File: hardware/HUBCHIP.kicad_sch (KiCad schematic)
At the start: 42 parts, among them Y1 25MHz

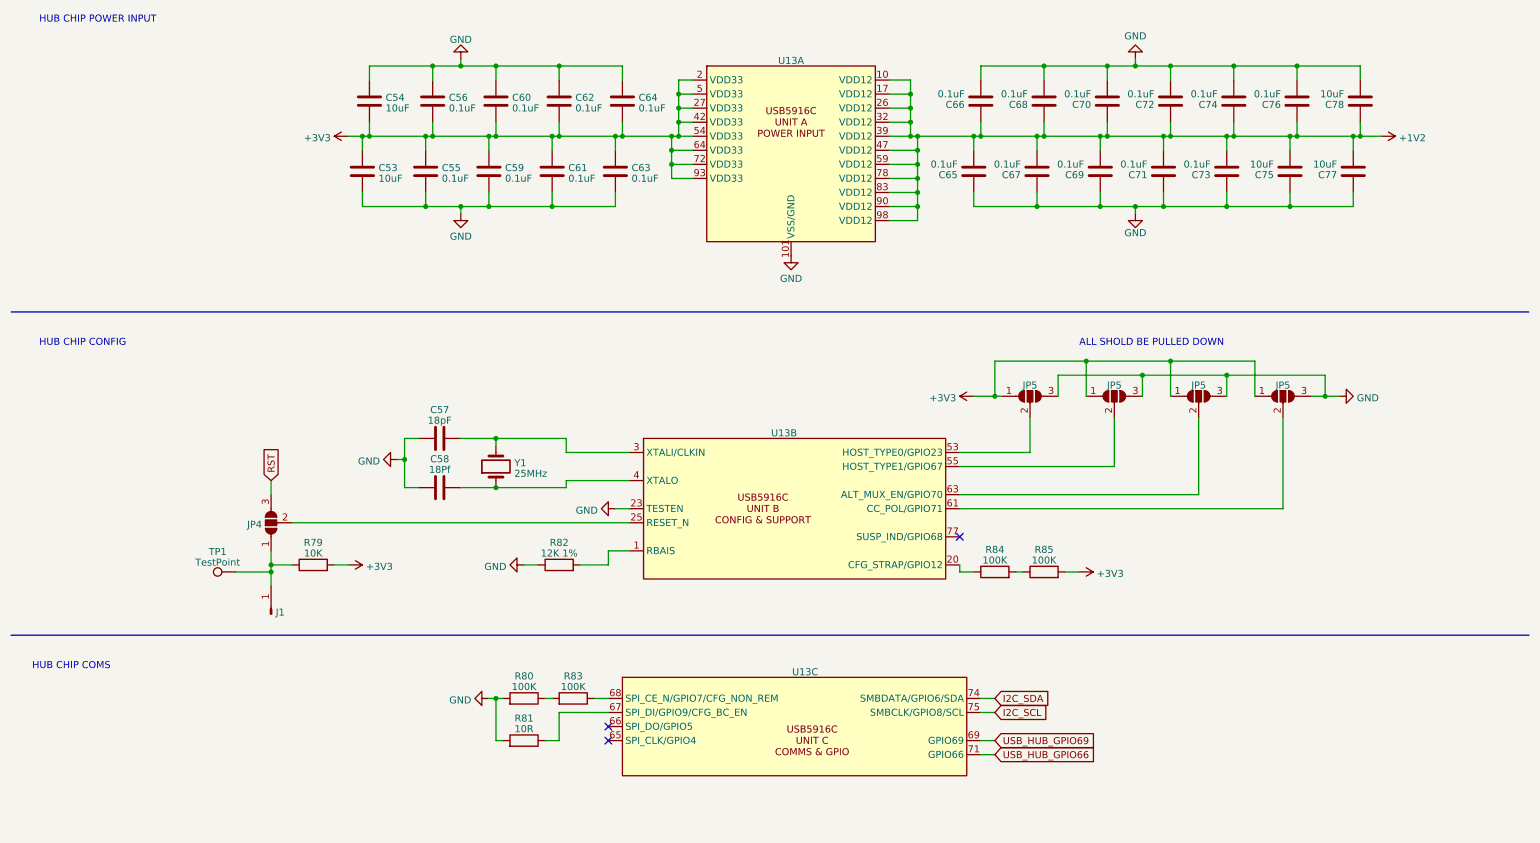
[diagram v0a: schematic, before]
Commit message: fixed DP issues and finneshed overall routeing
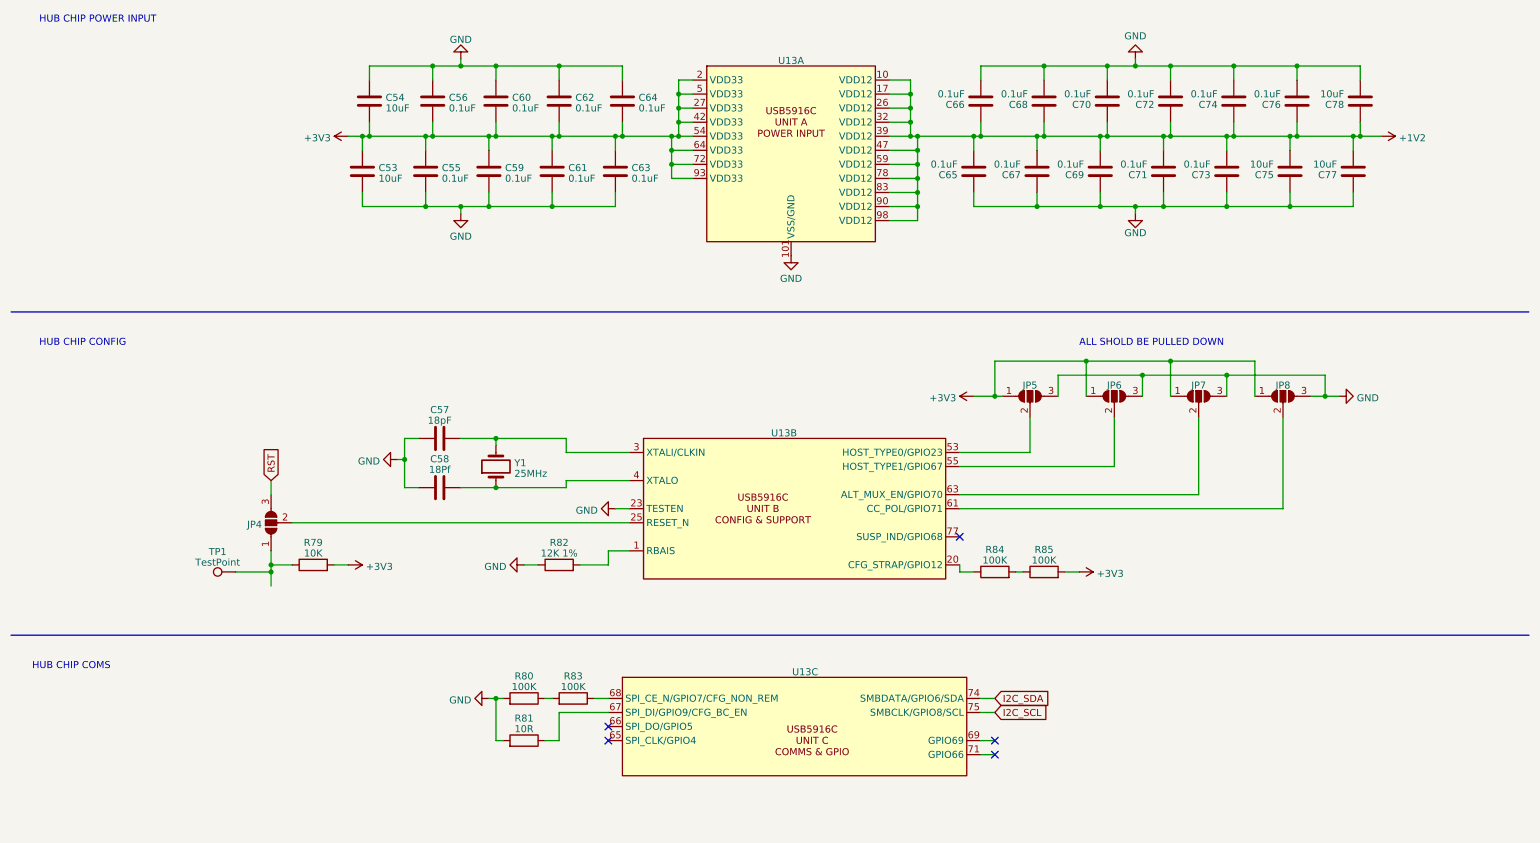
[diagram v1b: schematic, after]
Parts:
- removed J1: ~, Connector_PinHeader_2.54mm:PinHeader_1x01_P2.54mm_Vertical, symbol Connector:Conn_01x01_Pin
- renumbered JP5 to JP6, JP5 to JP7, JP5 to JP8
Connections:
- net USB_HUB_GPIO66: no longer names the net of U13.71 (GPIO66)
- net USB_HUB_GPIO69: no longer names the net of U13.69 (GPIO69)
- no-connect marks 3 -> 5
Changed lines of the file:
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@@
   (no_connect (at 119.38 147.32))
   (no_connect (at 182.88 110.49))
+  (no_connect (at 189.23 149.86))
+  (no_connect (at 189.23 147.32))
   (wire (pts (xy 86.36 48.26) (xy 86.36 50.8))
     (stroke (width 0) (type default))
@@
     )
   )
-  (global_label "USB_HUB_GPIO69" (shape input) (at 189.23 147.32 0) (fields_autoplaced)
-    (effects (font (size 1.27 1.27)) (justify left))
-    (property "Intersheetrefs" "${INTERSHEET_REFS}" (at 208.7063 147.32 0)
-      (effects (font (size 1.27 1.27)) (justify left) hide)
-    )
-  )
   (global_label "I2C_SCL" (shape input) (at 189.23 142.24 0) (fields_autoplaced)
     (effects (font (size 1.27 1.27)) (justify left))
@@
     )
   )
-  (global_label "USB_HUB_GPIO66" (shape input) (at 189.23 149.86 0) (fields_autoplaced)
-    (effects (font (size 1.27 1.27)) (justify left))
-    (property "Intersheetrefs" "${INTERSHEET_REFS}" (at 208.7063 149.86 0)
-      (effects (font (size 1.27 1.27)) (justify left) hide)
-    )
-  )
   (symbol (lib_id "Device:C") (at 185.42 44.45 180) (unit 1)
     (in_bom yes) (on_board yes) (dnp no)
@@
         (path "/fae025e9-99c5-40c1-af6f-99dc1edbfa43/7a7a6512-c96f-448a-bb8d-4d6e185adf7f"
           (reference "R85") (unit 1)
-        )
-      )
-    )
-  )
-  (symbol (lib_id "Connector:Conn_01x01_Pin") (at 58.42 124.46 90) (unit 1)
-    (in_bom yes) (on_board yes) (dnp no) (fields_autoplaced)
-    (property "Reference" "J1" (at 59.2582 124.1418 90)
-      (effects (font (size 1.27 1.27)) (justify right))
-    )
-    (property "Value" "~" (at 59.2582 125.1023 90)
-      (effects (font (size 1.27 1.27)) (justify right))
-    )
-    (property "Footprint" "Connector_PinHeader_2.54mm:PinHeader_1x01_P2.54mm_Vertical" (at 58.42 124.46 0)
-      (effects (font (size 1.27 1.27)) hide)
-    )
-    (property "Datasheet" "~" (at 58.42 124.46 0)
-      (effects (font (size 1.27 1.27)) hide)
-    )
-    (pin "1")
-    (instances
-      (project "usbc-car-module"
-        (path "/fae025e9-99c5-40c1-af6f-99dc1edbfa43/7a7a6512-c96f-448a-bb8d-4d6e185adf7f"
-          (reference "J1") (unit 1)
         )
       )
@@
   (symbol (lib_id "Jumper:SolderJumper_3_Open") (at 210.82 85.09 0) (unit 1)
     (in_bom yes) (on_board yes) (dnp no) (fields_autoplaced)
-    (property "Reference" "JP5" (at 210.82 83.1121 0)
+    (property "Reference" "JP6" (at 210.82 83.1121 0)
       (effects (font (size 1.27 1.27)))
     )
@@
     (instances
       (project "usbc-car-module"
-        (path "/fae025e9-99c5-40c1-af6f-99dc1edbfa43/bb20a659-2b02-48fa-8ef7-389a14e86ba7"
-          (reference "JP5") (unit 1)
-        )
-        (path "/fae025e9-99c5-40c1-af6f-99dc1edbfa43/ad0dde3f-c33d-40ce-8876-17a95cda421b"
-          (reference "JP10") (unit 1)
-        )
         (path "/fae025e9-99c5-40c1-af6f-99dc1edbfa43/7a7a6512-c96f-448a-bb8d-4d6e185adf7f"
           (reference "JP6") (unit 1)
@@
   (symbol (lib_id "Jumper:SolderJumper_3_Open") (at 241.3 85.09 0) (unit 1)
     (in_bom yes) (on_board yes) (dnp no) (fields_autoplaced)
-    (property "Reference" "JP5" (at 241.3 83.1121 0)
+    (property "Reference" "JP8" (at 241.3 83.1121 0)
       (effects (font (size 1.27 1.27)))
     )
@@
     (instances
       (project "usbc-car-module"
-        (path "/fae025e9-99c5-40c1-af6f-99dc1edbfa43/bb20a659-2b02-48fa-8ef7-389a14e86ba7"
-          (reference "JP5") (unit 1)
-        )
-        (path "/fae025e9-99c5-40c1-af6f-99dc1edbfa43/ad0dde3f-c33d-40ce-8876-17a95cda421b"
-          (reference "JP10") (unit 1)
-        )
         (path "/fae025e9-99c5-40c1-af6f-99dc1edbfa43/7a7a6512-c96f-448a-bb8d-4d6e185adf7f"
           (reference "JP8") (unit 1)
@@
   (symbol (lib_id "Jumper:SolderJumper_3_Open") (at 226.06 85.09 0) (unit 1)
     (in_bom yes) (on_board yes) (dnp no) (fields_autoplaced)
-    (property "Reference" "JP5" (at 226.06 83.1121 0)
+    (property "Reference" "JP7" (at 226.06 83.1121 0)
       (effects (font (size 1.27 1.27)))
     )
@@
     (instances
       (project "usbc-car-module"
-        (path "/fae025e9-99c5-40c1-af6f-99dc1edbfa43/bb20a659-2b02-48fa-8ef7-389a14e86ba7"
-          (reference "JP5") (unit 1)
-        )
-        (path "/fae025e9-99c5-40c1-af6f-99dc1edbfa43/ad0dde3f-c33d-40ce-8876-17a95cda421b"
-          (reference "JP10") (unit 1)
-        )
         (path "/fae025e9-99c5-40c1-af6f-99dc1edbfa43/7a7a6512-c96f-448a-bb8d-4d6e185adf7f"
           (reference "JP7") (unit 1)
@@
     (instances
       (project "usbc-car-module"
-        (path "/fae025e9-99c5-40c1-af6f-99dc1edbfa43/bb20a659-2b02-48fa-8ef7-389a14e86ba7"
+        (path "/fae025e9-99c5-40c1-af6f-99dc1edbfa43/7a7a6512-c96f-448a-bb8d-4d6e185adf7f"
           (reference "JP5") (unit 1)
-        )
-        (path "/fae025e9-99c5-40c1-af6f-99dc1edbfa43/ad0dde3f-c33d-40ce-8876-17a95cda421b"
-          (reference "JP10") (unit 1)
-        )
-        (path "/fae025e9-99c5-40c1-af6f-99dc1edbfa43/7a7a6512-c96f-448a-bb8d-4d6e185adf7f"
-          (reference "JP5") (unit 1)

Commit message: minor revisions
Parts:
- removed C57: 18pF, Capacitor_SMD:C_0603_1608Metric, symbol Device:C
- removed C58: 18Pf, Capacitor_SMD:C_0603_1608Metric, symbol Device:C
- removed Y1: 25MHz, Crystal:Crystal_SMD_HC49-SD, symbol Device:Crystal
- added X1: ECS-2033-250-BN, Oscillator:Oscillator_SMD_Kyocera_KC2520Z-4Pin_2.5x2.0mm, symbol Oscillator:TXC-7C
- U13: value ~ -> USB5926C
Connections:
- net +3V3: now also X1.1 (EN), X1.4 (Vdd)
- net GND: now also X1.2 (GND)
- net at U13.3 (XTALI/CLKIN): now also X1.3 (OUT)

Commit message: working on things
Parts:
- added TP16: TestPoint, TestPoint:TestPoint_Pad_D1.0mm, symbol Connector:TestPoint
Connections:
- net at U13.71 (GPIO66): now also TP16.1
- no-connect marks 5 -> 4
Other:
- moved on the sheet: TP1
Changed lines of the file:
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@@
   (junction (at 104.14 86.36) (diameter 0) (color 0 0 0 0)
-  )
-  (junction (at 58.42 116.84) (diameter 0) (color 0 0 0 0)
   )
   (junction (at 87.63 38.1) (diameter 0) (color 0 0 0 0)
@@
   (no_connect (at 119.38 147.32))
   (no_connect (at 182.88 110.49))
-  (no_connect (at 189.23 149.86))
   (no_connect (at 189.23 147.32))
   (wire (pts (xy 86.36 48.26) (xy 86.36 50.8))
@@
     (stroke (width 0) (type default))
   )
-  (wire (pts (xy 58.42 115.57) (xy 58.42 116.84))
+  (wire (pts (xy 58.42 115.57) (xy 58.42 119.38))
     (stroke (width 0) (type default))
   )
@@
     (stroke (width 0) (type default))
   )
-  (wire (pts (xy 58.42 116.84) (xy 58.42 119.38))
-    (stroke (width 0) (type default))
-  )
   (wire (pts (xy 100.33 147.32) (xy 99.06 147.32))
     (stroke (width 0) (type default))
@@
     (stroke (width 0) (type default))
   )
-  (wire (pts (xy 52.07 116.84) (xy 58.42 116.84))
+  (wire (pts (xy 52.07 119.38) (xy 58.42 119.38))
     (stroke (width 0) (type default))
   )
@@
     )
   )
+  (symbol (lib_id "Connector:TestPoint") (at 189.23 149.86 270) (unit 1)
+    (in_bom yes) (on_board yes) (dnp no)
+    (property "Reference" "TP16" (at 192.532 153.5049 90)
+      (effects (font (size 1.27 1.27)))
+    )
+    (property "Value" "TestPoint" (at 192.532 151.5839 90)
+      (effects (font (size 1.27 1.27)))
+    )
+    (property "Footprint" "TestPoint:TestPoint_Pad_D1.0mm" (at 189.23 154.94 0)
+      (effects (font (size 1.27 1.27)) hide)
+    )
+    (property "Datasheet" "~" (at 189.23 154.94 0)
+      (effects (font (size 1.27 1.27)) hide)
+    )
+    (pin "1")
+    (instances
+      (project "usbc-car-module"
+        (path "/fae025e9-99c5-40c1-af6f-99dc1edbfa43/7a7a6512-c96f-448a-bb8d-4d6e185adf7f"
+          (reference "TP16") (unit 1)
+        )
+      )
+    )
+  )
   (symbol (lib_id "power:GND") (at 92.71 105.41 270) (unit 1)
     (in_bom yes) (on_board yes) (dnp no) (fields_autoplaced)
@@
     )
   )
-  (symbol (lib_id "Connector:TestPoint") (at 52.07 116.84 90) (unit 1)
-    (in_bom yes) (on_board yes) (dnp no) (fields_autoplaced)
-    (property "Reference" "TP1" (at 48.768 113.1951 90)
-      (effects (font (size 1.27 1.27)))
-    )
-    (property "Value" "TestPoint" (at 48.768 115.1161 90)
-      (effects (font (size 1.27 1.27)))
-    )
-    (property "Footprint" "TestPoint:TestPoint_Pad_D1.0mm" (at 52.07 111.76 0)
-      (effects (font (size 1.27 1.27)) hide)
-    )
-    (property "Datasheet" "~" (at 52.07 111.76 0)
-      (effects (font (size 1.27 1.27)) hide)
-    )
+  (symbol (lib_id "Connector:TestPoint") (at 52.07 119.38 90) (unit 1)
+    (in_bom yes) (on_board yes) (dnp no)
+    (property "Reference" "TP1" (at 48.768 115.7351 90)
+      (effects (font (size 1.27 1.27)))
+    )
+    (property "Value" "TestPoint" (at 48.768 117.6561 90)
+      (effects (font (size 1.27 1.27)))
+    )
+    (property "Footprint" "TestPoint:TestPoint_Pad_D1.0mm" (at 52.07 114.3 0)
+      (effects (font (size 1.27 1.27)) hide)
+    )
+    (property "Datasheet" "~" (at 52.07 114.3 0)
+      (effects (font (size 1.27 1.27)) hide)
+    )

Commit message: switched can tranceiver to combo controler and tranceiver
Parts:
- added TP18, TP23, TP24, TP25: TestPoint, TestPoint:TestPoint_Pad_D1.0mm, symbol Connector:TestPoint
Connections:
- net at U13.65 (SPI_CLK/GPIO4): now also TP23.1
- net at U13.66 (SPI_DO/GPIO5): now also TP24.1
- net at U13.69 (GPIO69): now also TP18.1
- net at U13.77 (SUSP_IND/GPIO68): now also TP25.1
- no-connect marks 4 -> 0

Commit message: kicad version upgrade and minor pcb changes
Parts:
- removed TP1: TestPoint, TestPoint:TestPoint_Pad_D1.0mm, symbol Connector:TestPoint
- added TP48: TestPoint, TestPoint:TestPoint_Pad_D1.0mm, symbol Connector:TestPoint
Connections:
- net at U13.3 (XTALI/CLKIN), X1.3 (OUT): now also TP48.1
- no-connect marks 0 -> 1
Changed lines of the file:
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@@
 	)
 	(junction
+		(at 118.11 95.25)
+		(diameter 0)
+		(color 0 0 0 0)
+	)
+	(junction
 		(at 173.99 30.48)
 		(diameter 0)
@@
 	)
 	(junction
-		(at 58.42 115.57)
-		(diameter 0)
-		(color 0 0 0 0)
-	)
-	(junction
 		(at 175.26 38.1)
 		(diameter 0)
@@
 		(color 0 0 0 0)
 	)
+	(no_connect
+		(at 123.19 100.33)
+	)
 	(wire
 		(pts
@@
 	(wire
 		(pts
-			(xy 123.19 95.25) (xy 111.76 95.25)
+			(xy 123.19 95.25) (xy 118.11 95.25)
 		)
 		(stroke
@@
 	(wire
 		(pts
-			(xy 58.42 115.57) (xy 58.42 119.38)
-		)
-		(stroke
-			(width 0)
-			(type default)
-		)
-	)
-	(wire
-		(pts
 			(xy 175.26 53.34) (xy 175.26 50.8)
 		)
@@
 	(wire
 		(pts
+			(xy 118.11 87.63) (xy 118.11 95.25)
+		)
+		(stroke
+			(width 0)
+			(type default)
+		)
+	)
+	(wire
+		(pts
 			(xy 100.33 147.32) (xy 99.06 147.32)
 		)
@@
 	(wire
 		(pts
+			(xy 118.11 95.25) (xy 111.76 95.25)
+		)
+		(stroke
+			(width 0)
+			(type default)
+		)
+	)
+	(wire
+		(pts
 			(xy 132.08 35.56) (xy 134.62 35.56)
 		)
@@
 	(wire
 		(pts
-			(xy 52.07 119.38) (xy 58.42 119.38)
-		)
-		(stroke
-			(width 0)
-			(type default)
-		)
-	)
-	(wire
-		(pts
 			(xy 214.63 50.8) (xy 208.28 50.8)
 		)
@@
 	)
 	(symbol
+		(lib_id "Connector:TestPoint")
+		(at 118.11 87.63 0)
+		(unit 1)
+		(exclude_from_sim no)
+		(in_bom yes)
+		(on_board yes)
+		(dnp no)
+		(property "Reference" "TP48"
+			(at 119.507 84.6448 0)
+			(effects
+				(font
+					(size 1.27 1.27)
+				)
+				(justify left)
+			)
+		)
+		(property "Value" "TestPoint"
+			(at 119.38 86.36 0)
+			(effects
+				(font
+					(size 1.27 1.27)
+				)
+				(justify left)
+			)
+		)
+		(property "Footprint" "TestPoint:TestPoint_Pad_D1.0mm"
+			(at 123.19 87.63 0)
+			(effects
+				(font
+					(size 1.27 1.27)
+				)
+				(hide yes)
+			)
+		)
+		(property "Datasheet" "~"
+			(at 123.19 87.63 0)
+			(effects
+				(font
+					(size 1.27 1.27)
+				)
+				(hide yes)
+			)
+		)
+		(property "Description" ""
+			(at 118.11 87.63 0)
+			(effects
+				(font
+					(size 1.27 1.27)
+				)
+				(hide yes)
+			)
+		)
+		(pin "1"
+		)
+		(instances
+			(project "usbc-car-module"
+				(path "/fae025e9-99c5-40c1-af6f-99dc1edbfa43/7a7a6512-c96f-448a-bb8d-4d6e185adf7f"
+					(reference "TP48")
+					(unit 1)
+				)
+			)
+		)
+	)
+	(symbol
 		(lib_id "Device:C")
 		(at 220.98 31.75 180)
@@
 					(unit 1)
 				)
-			)
-		)
-	)
-	(symbol
-		(lib_id "Connector:TestPoint")
-		(at 52.07 119.38 90)
-		(unit 1)
-		(exclude_from_sim no)
-		(in_bom yes)
-		(on_board yes)
-		(dnp no)
-		(property "Reference" "TP1"
-			(at 48.768 115.7351 90)
-			(effects
-				(font
-					(size 1.27 1.27)
-				)
-			)
-		)
-		(property "Value" "TestPoint"
-			(at 48.768 117.6561 90)
-			(effects
-				(font
-					(size 1.27 1.27)
-				)
-			)
-		)
-		(property "Footprint" "TestPoint:TestPoint_Pad_D1.0mm"
-			(at 52.07 114.3 0)
-			(effects
-				(font
-					(size 1.27 1.27)
-				)
-				(hide yes)
-			)
-		)
-		(property "Datasheet" "~"
-			(at 52.07 114.3 0)
-			(effects
-				(font
-					(size 1.27 1.27)
-				)
-				(hide yes)
-			)
-		)
-		(property "Description" ""
-			(at 52.07 119.38 0)
-			(effects
-				(font
-					(size 1.27 1.27)
-				)
-				(hide yes)
-			)
-		)
-		(pin "1"
-		)
-		(instances
-			(project "usbc-car-module"
-				(path "/fae025e9-99c5-40c1-af6f-99dc1edbfa43/7a7a6512-c96f-448a-bb8d-4d6e185adf7f"
-					(reference "TP1")
-					(unit 1)
-				)
